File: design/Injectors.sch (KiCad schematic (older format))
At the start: 20 parts

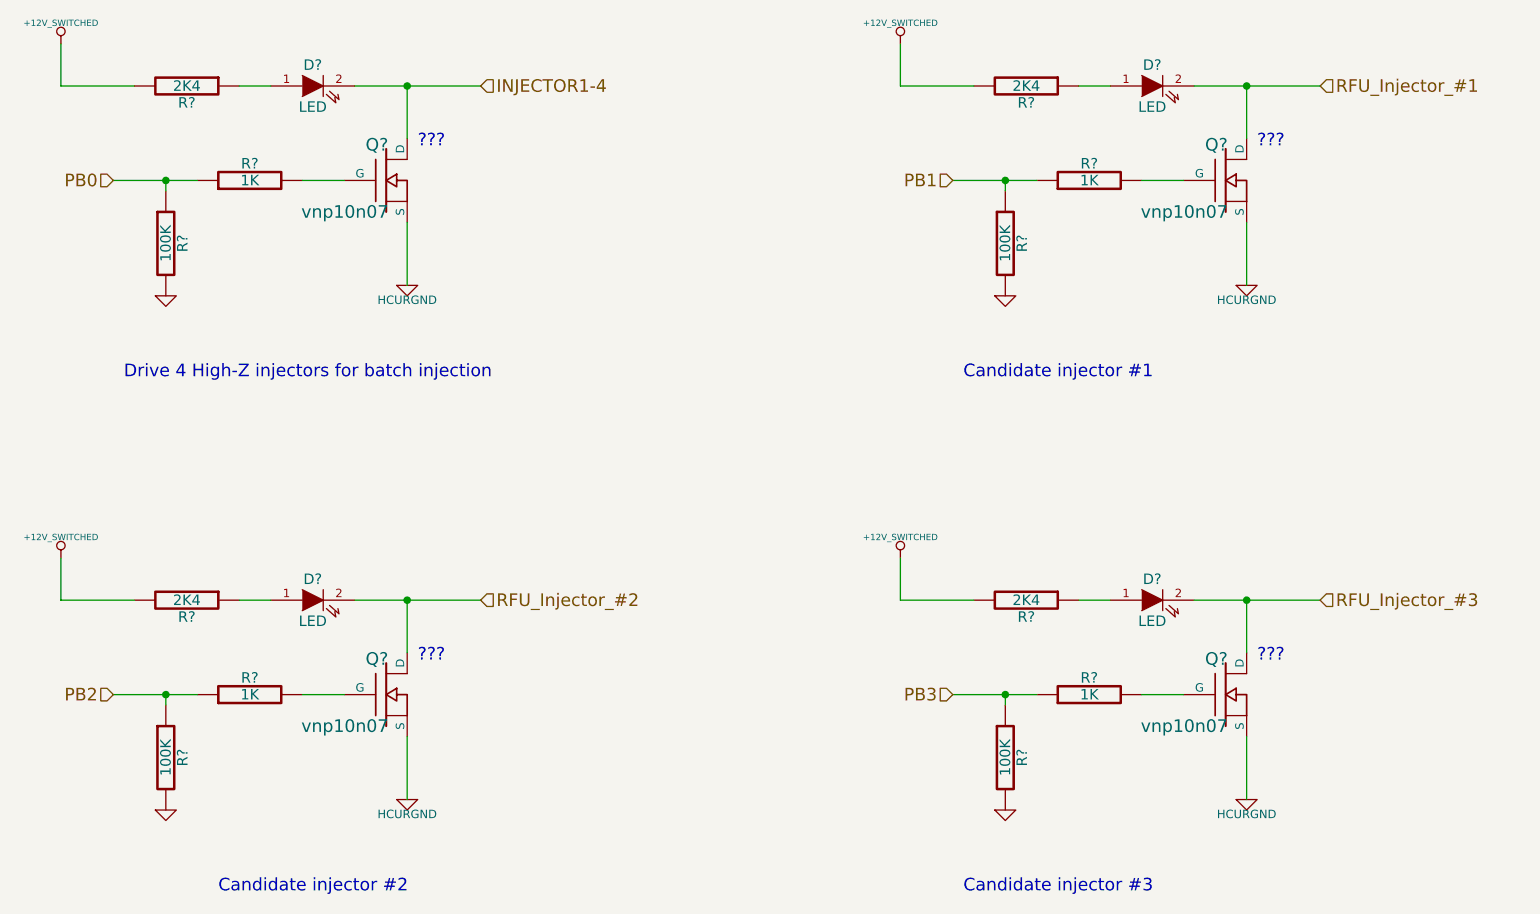
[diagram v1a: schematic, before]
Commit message: decide to put CPU on mainboard, drop core board design
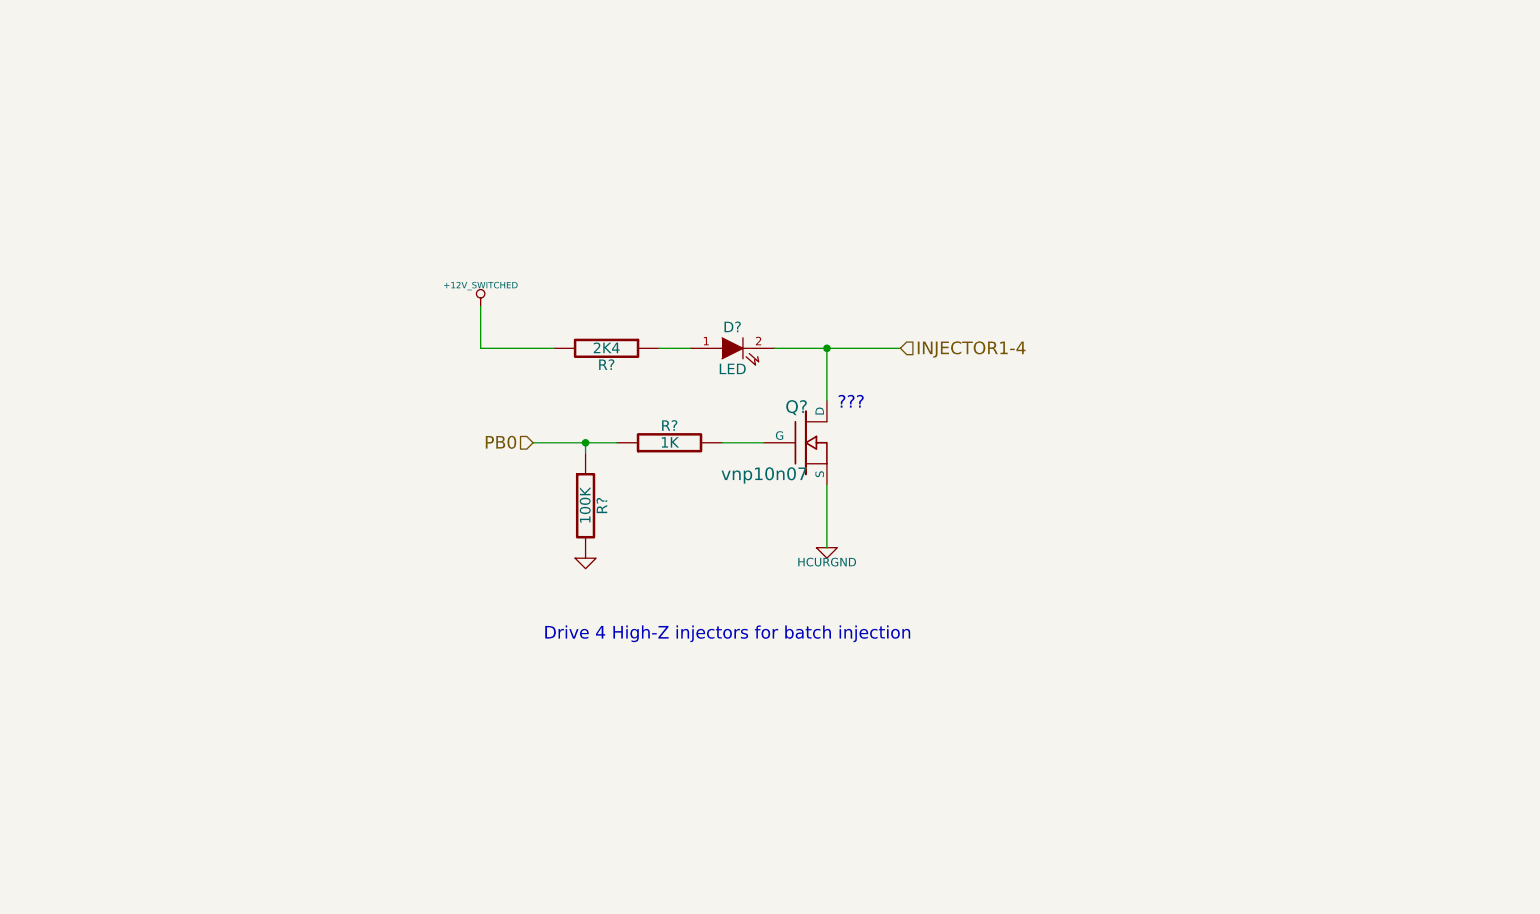
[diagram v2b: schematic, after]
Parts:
- removed D? (x3): LED, symbol LED
- removed Q? (x3): vnp10n07, symbol MOS_N
- removed R? (x3): 1K, symbol R
- removed R? (x3): 100K, symbol R
- removed R? (x3): 2K4, symbol R
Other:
- note removed: "Candidate injector #1"
- note removed: "Candidate injector #2"
- note removed: "Candidate injector #3"
- moved on the sheet: D?, Q?, R?

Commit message: revise schema to be full pin compatible with stock ECU
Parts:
- gave numbers to parts that had none: 5
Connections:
- net labels added: LSGND
- net labels removed: HCURGND
- wire segments 11 -> 9
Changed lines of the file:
@@
-EESchema Schematic File Version 2  date 27/12/2011 00:52:12
+EESchema Schematic File Version 2  date 02/01/2012 14:25:41
 LIBS:power
 LIBS:device
@@
 EELAYER END
 $Descr A4 11700 8267
-Sheet 10 12
+Sheet 11 12
 Title "batch injection"
-Date "26 dec 2011"
+Date "2 jan 2012"
 Rev "0.01"
 Comp "diyefi.org"
@@
 $EndDescr
 $Comp
-L +12V_SWITCHED #PWR?
+L LSGND #PWR097
+U 1 1 4EFDEB71
+P 6050 4200
+F 0 "#PWR097" H 6050 4200 40  0001 C CNN
+F 1 "LSGND" H 6050 4130 40  0000 C CNN
+	1    6050 4200
+	1    0    0    -1
+$EndComp
+$Comp
+L +12V_SWITCHED #PWR098
 U 1 1 4E924AFA
 P 4400 3050
-F 0 "#PWR?" H 4400 3000 20  0001 C CNN
+F 0 "#PWR098" H 4400 3000 20  0001 C CNN
 F 1 "+12V_SWITCHED" H 4400 3150 30  0000 C CNN
 	1    4400 3050
@@
 Drive 4 High-Z injectors for batch injection
 $Comp
-L MOS_N Q?
+L MOS_N Q9
 U 1 1 4E919ABF
 P 5950 3700
-F 0 "Q?" H 5960 3870 60  0000 R CNN
+F 0 "Q9" H 5960 3870 60  0000 R CNN
 F 1 "vnp10n07" H 5960 3550 60  0000 R CNN
 	1    5950 3700
@@
 $EndComp
 $Comp
-L R R?
+L R R67
 U 1 1 4E919ABE
 P 5300 3700
-F 0 "R?" V 5380 3700 50  0000 C CNN
+F 0 "R67" V 5380 3700 50  0000 C CNN
 F 1 "1K" V 5300 3700 50  0000 C CNN
 	1    5300 3700
@@
 INJECTOR1-4
 $Comp
-L HCURGND #PWR?
-U 1 1 4E919ABD
-P 6050 4200
-F 0 "#PWR?" H 6050 4200 40  0001 C CNN
-F 1 "HCURGND" H 6050 4130 40  0000 C CNN
-	1    6050 4200
-	1    0    0    -1
-$EndComp
-$Comp
-L R R?
+L R R68
 U 1 1 4E919ABC
 P 4900 4000
-F 0 "R?" V 4980 4000 50  0000 C CNN
+F 0 "R68" V 4980 4000 50  0000 C CNN
 F 1 "100K" V 4900 4000 50  0000 C CNN
 	1    4900 4000
@@
 $EndComp
 $Comp
-L GND #PWR?
+L GND #PWR099
 U 1 1 4E919ABB
 P 4900 4250
-F 0 "#PWR?" H 4900 4250 30  0001 C CNN
+F 0 "#PWR099" H 4900 4250 30  0001 C CNN
 F 1 "GND" H 4900 4180 30  0001 C CNN
 	1    4900 4250
@@
 $EndComp
 $Comp
-L LED D?
+L LED D27
 U 1 1 4E919ABA
 P 5600 3250
-F 0 "D?" H 5600 3350 50  0000 C CNN
+F 0 "D27" H 5600 3350 50  0000 C CNN
 F 1 "LED" H 5600 3150 50  0000 C CNN
 	1    5600 3250
@@
 $EndComp
 $Comp
-L R R?
+L R R66
 U 1 1 4E919AB9
 P 5000 3250
-F 0 "R?" V 5080 3250 50  0000 C CNN
+F 0 "R66" V 5080 3250 50  0000 C CNN
 F 1 "2K4" V 5000 3250 50  0000 C CNN
 	1    5000 3250
@@
 $EndComp
 Wire Wire Line
-	4400 3250 4400 3050
+	4400 3050 4400 3250
 Wire Wire Line
-	4750 3250 4400 3250
+	4400 3250 4750 3250
 Wire Wire Line
-	5800 3250 6050 3250
-Wire Wire Line
-	6050 3250 6400 3250
+	5800 3250 6400 3250
 Wire Wire Line
 	6050 4200 6050 3900
 Wire Wire Line
-	5050 3700 4900 3700
-Wire Wire Line
-	4900 3700 4650 3700
+	5050 3700 4650 3700
 Wire Wire Line
 	5550 3700 5750 3700

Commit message: add test points on critical output, resolve all kind of DRC issue, generate a netlist
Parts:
- added W7: TEST, symbol TEST
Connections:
- wire segments 9 -> 12
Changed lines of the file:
@@
-EESchema Schematic File Version 2  date 02/01/2012 14:25:41
+EESchema Schematic File Version 2  date 03/01/2012 09:04:48
 LIBS:power
 LIBS:device
@@
 Sheet 11 12
 Title "batch injection"
-Date "2 jan 2012"
+Date "3 jan 2012"
 Rev "0.01"
 Comp "diyefi.org"
@@
 Comment4 ""
 $EndDescr
+Wire Wire Line
+	4250 4250 4250 4100
+Wire Wire Line
+	4400 3050 4400 3250
+Wire Wire Line
+	4400 3250 4750 3250
+Wire Wire Line
+	6400 3250 5800 3250
+Wire Wire Line
+	6050 4200 6050 3900
+Wire Wire Line
+	4650 3700 5050 3700
+Wire Wire Line
+	5550 3700 5750 3700
+Connection ~ 4900 3700
+Wire Wire Line
+	5250 3250 5400 3250
+Wire Wire Line
+	6050 3500 6050 3250
+Connection ~ 6050 3250
+Wire Wire Line
+	4250 3700 4250 3500
+Wire Wire Line
+	4250 3500 4900 3500
+Wire Wire Line
+	4900 3500 4900 3750
 $Comp
-L LSGND #PWR097
+L GND #PWR104
+U 1 1 4F01C391
+P 4250 4250
+F 0 "#PWR104" H 4250 4250 30  0001 C CNN
+F 1 "GND" H 4250 4180 30  0001 C CNN
+	1    4250 4250
+	1    0    0    -1
+$EndComp
+$Comp
+L TEST W7
+U 1 1 4F01C365
+P 4250 3900
+F 0 "W7" H 4250 3960 40  0000 C CNN
+F 1 "TEST" H 4250 3830 40  0000 C CNN
+	1    4250 3900
+	0    1    1    0
+$EndComp
+$Comp
+L LSGND #PWR103
 U 1 1 4EFDEB71
 P 6050 4200
-F 0 "#PWR097" H 6050 4200 40  0001 C CNN
+F 0 "#PWR103" H 6050 4200 40  0001 C CNN
 F 1 "LSGND" H 6050 4130 40  0000 C CNN
 	1    6050 4200
@@
 $EndComp
 $Comp
-L +12V_SWITCHED #PWR098
+L +12V_SWITCHED #PWR102
 U 1 1 4E924AFA
 P 4400 3050
-F 0 "#PWR098" H 4400 3000 20  0001 C CNN
+F 0 "#PWR102" H 4400 3000 20  0001 C CNN
 F 1 "+12V_SWITCHED" H 4400 3150 30  0000 C CNN
 	1    4400 3050
@@
 $EndComp
 $Comp
-L GND #PWR099
+L GND #PWR105
 U 1 1 4E919ABB
 P 4900 4250
-F 0 "#PWR099" H 4900 4250 30  0001 C CNN
+F 0 "#PWR105" H 4900 4250 30  0001 C CNN
 F 1 "GND" H 4900 4180 30  0001 C CNN
 	1    4900 4250
@@
 	0    1    1    0
 $EndComp
-Wire Wire Line
-	4400 3050 4400 3250
-Wire Wire Line
-	4400 3250 4750 3250
-Wire Wire Line
-	5800 3250 6400 3250
-Wire Wire Line
-	6050 4200 6050 3900
-Wire Wire Line
-	5050 3700 4650 3700
-Wire Wire Line
-	5550 3700 5750 3700
-Wire Wire Line
-	4900 3750 4900 3700
-Connection ~ 4900 3700
-Wire Wire Line
-	5250 3250 5400 3250
-Wire Wire Line
-	6050 3500 6050 3250
-Connection ~ 6050 3250
 $EndSCHEMATC

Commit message: add missing diodes, re-generate netlist, assign all footprints, ready to layout
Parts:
- added D34: DIODE, symbol DIODE
- renumbered D27 to D33
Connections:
- wire segments 12 -> 14
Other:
- note removed: "???"
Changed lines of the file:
@@
-EESchema Schematic File Version 2  date 03/01/2012 09:04:48
+EESchema Schematic File Version 2  date 12/01/2012 20:05:35
 LIBS:power
 LIBS:device
@@
 Sheet 11 12
 Title "batch injection"
-Date "3 jan 2012"
+Date "12 jan 2012"
 Rev "0.01"
 Comp "diyefi.org"
@@
 Comment4 ""
 $EndDescr
+Wire Wire Line
+	6300 3900 6050 3900
 Wire Wire Line
 	4250 4250 4250 4100
@@
 	6400 3250 5800 3250
 Wire Wire Line
-	6050 4200 6050 3900
+	6050 3900 6050 4200
 Wire Wire Line
 	4650 3700 5050 3700
@@
 	5250 3250 5400 3250
 Wire Wire Line
-	6050 3500 6050 3250
+	6050 3250 6050 3500
 Connection ~ 6050 3250
 Wire Wire Line
@@
 Wire Wire Line
 	4900 3500 4900 3750
+Wire Wire Line
+	6050 3500 6300 3500
+$Comp
+L DIODE D34
+U 1 1 4F0EC8E1
+P 6300 3700
+F 0 "D34" H 6300 3800 40  0000 C CNN
+F 1 "DIODE" H 6300 3600 40  0000 C CNN
+	1    6300 3700
+	0    -1   -1   0
+$EndComp
 $Comp
 L GND #PWR104
@@
 Text HLabel 4650 3700 0    60   Input ~ 0
 PB0
-Text Notes 6100 3550 0    60   ~ 0
-???
 Text HLabel 6400 3250 2    60   Input ~ 0
 INJECTOR1-4
@@
 $EndComp
 $Comp
-L LED D27
+L LED D33
 U 1 1 4E919ABA
 P 5600 3250
-F 0 "D27" H 5600 3350 50  0000 C CNN
+F 0 "D33" H 5600 3350 50  0000 C CNN
 F 1 "LED" H 5600 3150 50  0000 C CNN
 	1    5600 3250
